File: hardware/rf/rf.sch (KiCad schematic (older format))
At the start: 47 parts, among them J1 Conn_02x14_Odd_Even, J2 SMP, J3 SMP, J4 SMP, U1 ECS-2520S33-400, U2 LMX2491, U3 BGT24MTR12

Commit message: Added BGT24 module castellation footprint, 3d model for 40MHz XO. Edits to schematic and pinouts based on layout of module. Initial parts placement and routing complete.
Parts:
- removed J1: Conn_02x14_Odd_Even, symbol Connector_Generic:Conn_02x14_Odd_Even
- removed R1, R3, R9: 0, Resistor_SMD:R_0402_1005Metric, symbol Device:R_US
- added J1: BGT24_Module_Castellations, bloop:BGT24_Module_Castellations, symbol bloop:BGT24_Module_Castellations
- C1, C12, C13, C15, C16, C17, C18, C2, C20, C21, C24, C25, C3, C4, C5, C6, C7, C8, C9: footprint Capacitor_SMD:C_0402_1005Metric -> Capacitor_SMD:C_0201_0603Metric
- R10, R2, R4, R5, R7, R8: footprint Resistor_SMD:R_0402_1005Metric -> Capacitor_SMD:C_0201_0603Metric
- R6: footprint Resistor_SMD:R_0402_1005Metric -> Capacitor_SMD:C_0402_1005Metric
- U1: footprint Crystal:Crystal_SMD_2520-4Pin_2.5x2.0mm -> bloop:Crystal_SMD_2520-4Pin_2.5x2.0mm
- U2: footprint Package_DFN_QFN:VQFN-24-1EP_4x4mm_P0.5mm_EP2.45x2.45mm -> Package_DFN_QFN:VQFN-24-1EP_4x4mm_P0.5mm_EP2.45x2.45mm_ThermalVias
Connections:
- wire segments 271 -> 259
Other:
- note added: "IF1 I/Q"
- note added: "IF2 I/Q"
- note added: "RF and PLL \npower isolated"
- note removed: "I/Q"
- moved on the sheet: C12, C14, C19, C20, C21, FB1, FB2, FB3

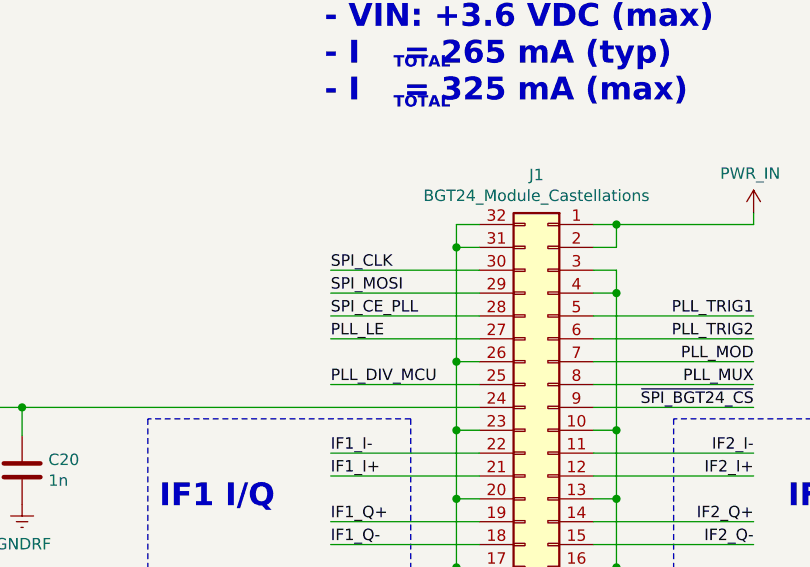
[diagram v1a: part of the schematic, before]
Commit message: Added 85305-0232 footprint for SMT SMP connector
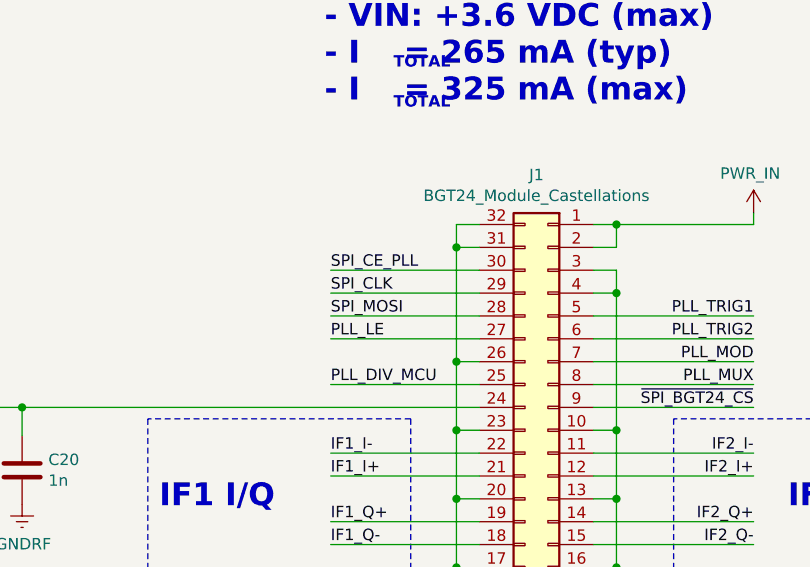
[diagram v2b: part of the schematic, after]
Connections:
- net SPI_CE_PLL: now also J1.30 (Pin_30); no longer J1.28 (Pin_28)
- net SPI_CLK: now also J1.29 (Pin_29); no longer J1.30 (Pin_30)
- net SPI_MOSI: now also J1.28 (Pin_28); no longer J1.29 (Pin_29)
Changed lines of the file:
@@
 Wire Wire Line
 	7750 2600 7975 2600
+Text Label 8800 7450 0    50   ~ 0
+SPI_CE_PLL
+Text Label 8800 7550 0    50   ~ 0
+SPI_CLK
 Text Label 8800 7650 0    50   ~ 0
-SPI_CE_PLL
-Text Label 8800 7450 0    50   ~ 0
-SPI_CLK
-Text Label 8800 7550 0    50   ~ 0
 SPI_MOSI
 Text Label 8800 7750 0    50   ~ 0
@@
 Connection ~ 9350 8750
 Wire Wire Line
-	8800 7550 9450 7550
-Wire Wire Line
-	9450 7450 8800 7450
-Wire Wire Line
 	8800 7650 9450 7650
 Wire Wire Line
+	9450 7550 8800 7550
+Wire Wire Line
+	8800 7450 9450 7450
+Wire Wire Line
 	9450 7750 8800 7750

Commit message: Replaced TH SMP connectors with SMT
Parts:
- J2, J3, J4: footprint bloop:0734153320 -> bloop:85305-0232
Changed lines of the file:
@@
 F 0 "J2" H 15957 3201 50  0000 L CNN
 F 1 "SMP" H 16060 2920 50  0000 L CNN
-F 2 "bloop:0734153320" H 16000 3050 50  0001 C CNN
+F 2 "bloop:85305-0232" H 16000 3050 50  0001 C CNN
 F 3 " ~" H 16000 3050 50  0001 C CNN
 	1    16000 3050
@@
 F 0 "J3" H 15957 3951 50  0000 L CNN
 F 1 "SMP" H 16060 3670 50  0000 L CNN
-F 2 "bloop:0734153320" H 16000 3800 50  0001 C CNN
+F 2 "bloop:85305-0232" H 16000 3800 50  0001 C CNN
 F 3 " ~" H 16000 3800 50  0001 C CNN
 	1    16000 3800
@@
 F 0 "J4" H 15957 4751 50  0000 L CNN
 F 1 "SMP" H 16060 4470 50  0000 L CNN
-F 2 "bloop:0734153320" H 16000 4600 50  0001 C CNN
+F 2 "bloop:85305-0232" H 16000 4600 50  0001 C CNN
 F 3 " ~" H 16000 4600 50  0001 C CNN
 	1    16000 4600

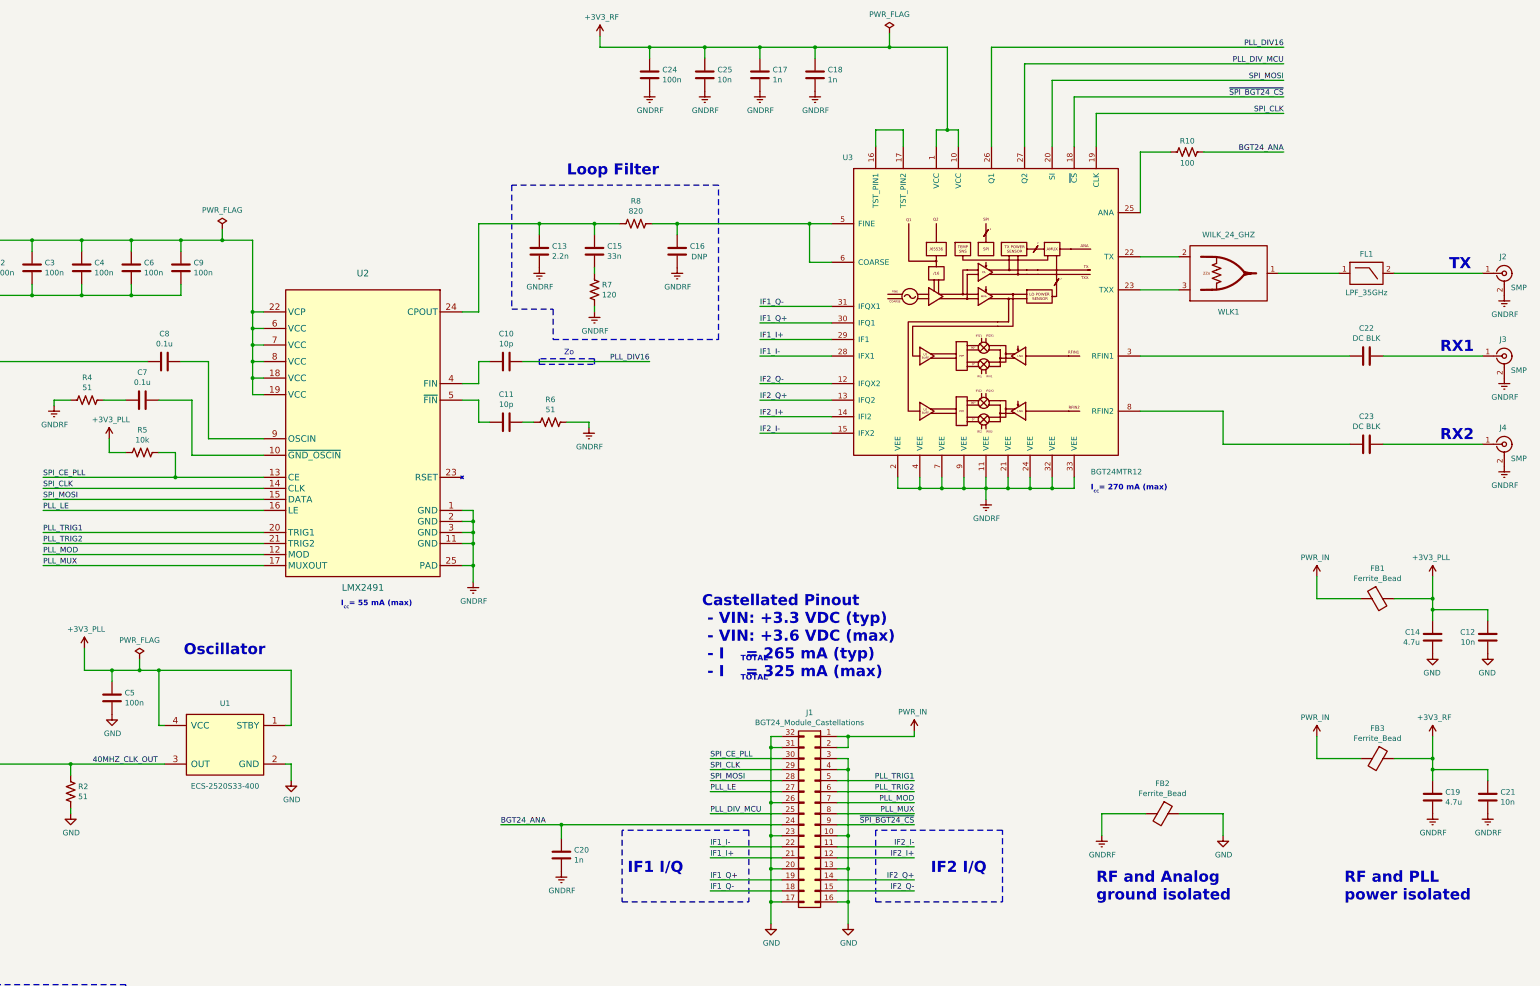
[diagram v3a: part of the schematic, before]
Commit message: Add 30 mil mask; update schematic for connector orientation
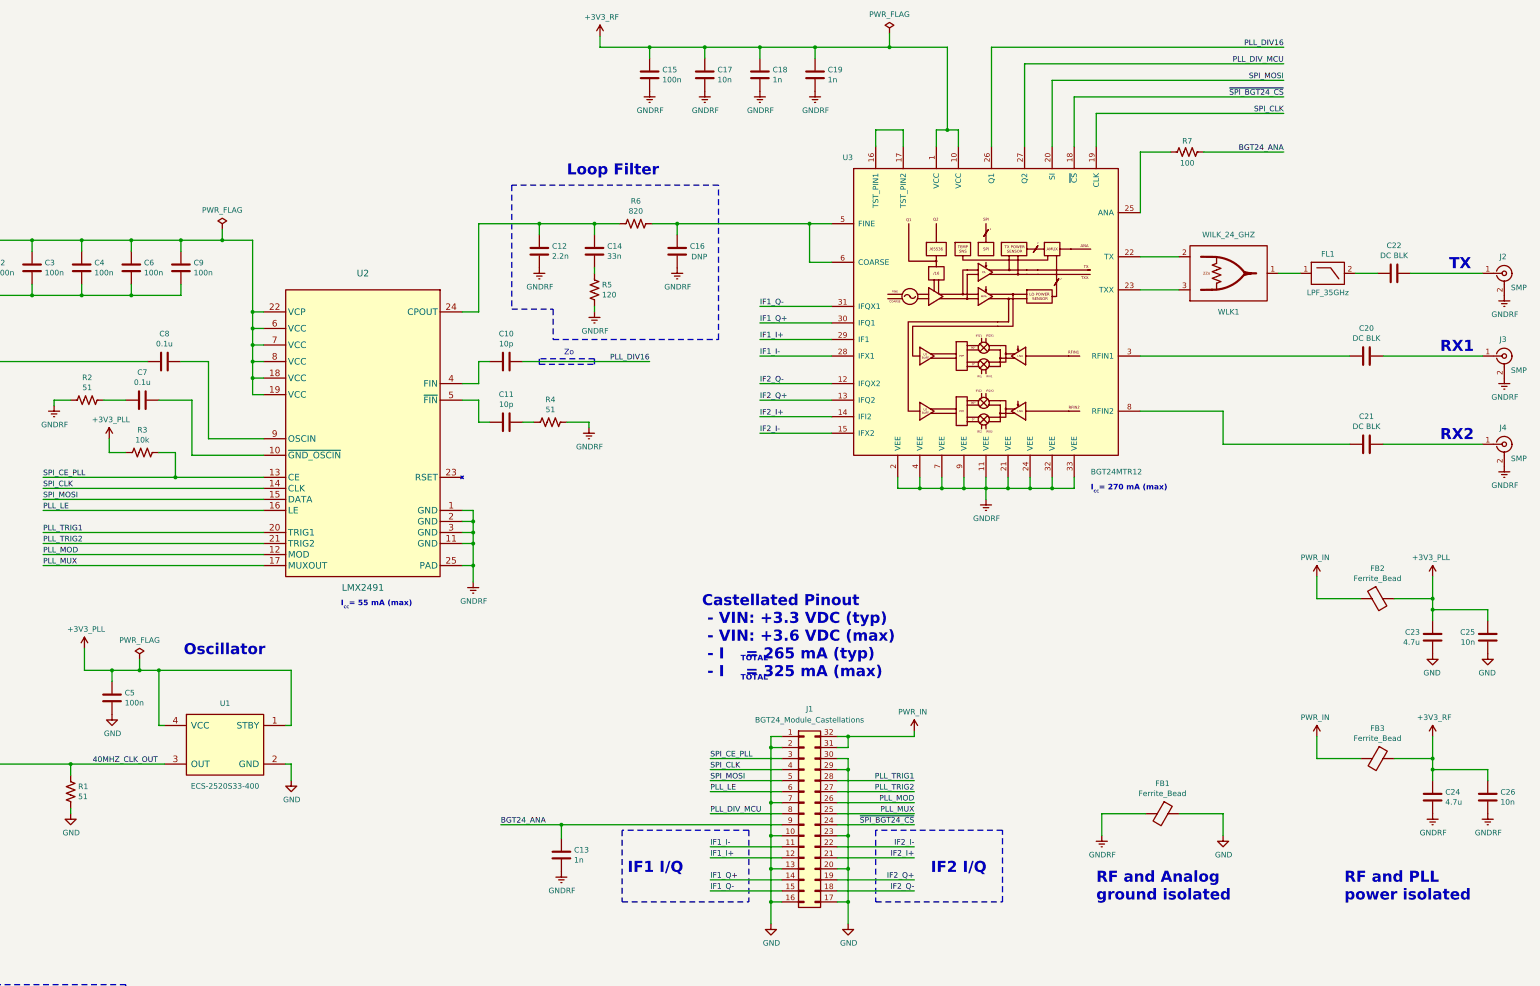
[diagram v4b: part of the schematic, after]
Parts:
- added C22: DC BLK, bloop:DC_Block, symbol Device:C
- renumbered C13 to C12, C20 to C13, C15 to C14, C24 to C15, C25 to C17, C17 to C18, C18 to C19, C22 to C20, C23 to C21, C14 to C23, C19 to C24, C12 to C25, C21 to C26, FB2 to FB1, FB1 to FB2, R2 to R1, R4 to R2, R5 to R3, R6 to R4, R7 to R5, R8 to R6, R10 to R7
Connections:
- net BGT24_ANA: now also J1.9 (Pin_9); no longer J1.24 (Pin_24)
- net GND: now also J1.1 (Pin_1), J1.2 (Pin_2), J1.29 (Pin_29), J1.30 (Pin_30), J1.7 (Pin_7); no longer J1.26 (Pin_26), J1.3 (Pin_3), J1.31 (Pin_31), J1.32 (Pin_32), J1.4 (Pin_4)
- net IF1_I+: now also J1.12 (Pin_12); no longer J1.21 (Pin_21)
- net IF1_I-: now also J1.11 (Pin_11); no longer J1.22 (Pin_22)
- net IF1_Q+: now also J1.14 (Pin_14); no longer J1.19 (Pin_19)
- net IF1_Q-: now also J1.15 (Pin_15); no longer J1.18 (Pin_18)
- net IF2_I+: now also J1.21 (Pin_21); no longer J1.12 (Pin_12)
- net IF2_I-: now also J1.22 (Pin_22); no longer J1.11 (Pin_11)
- net IF2_Q+: now also J1.19 (Pin_19); no longer J1.14 (Pin_14)
- net IF2_Q-: now also J1.18 (Pin_18); no longer J1.15 (Pin_15)
- net PLL_DIV_MCU: now also J1.8 (Pin_8); no longer J1.25 (Pin_25)
- net PLL_LE: now also J1.6 (Pin_6); no longer J1.27 (Pin_27)
- net PLL_MOD: now also J1.26 (Pin_26); no longer J1.7 (Pin_7)
- net PLL_MUX: now also J1.25 (Pin_25); no longer J1.8 (Pin_8)
- net PLL_TRIG1: now also J1.28 (Pin_28); no longer J1.5 (Pin_5)
- net PLL_TRIG2: now also J1.27 (Pin_27); no longer J1.6 (Pin_6)
- net PWR_IN: now also J1.31 (Pin_31), J1.32 (Pin_32); no longer J1.1 (Pin_1), J1.2 (Pin_2)
- net SPI_CE_PLL: now also J1.3 (Pin_3); no longer J1.30 (Pin_30)
- net SPI_CLK: now also J1.4 (Pin_4); no longer J1.29 (Pin_29)
- net SPI_MOSI: now also J1.5 (Pin_5); no longer J1.28 (Pin_28)
- net ~SPI_BGT24_CS: now also J1.24 (Pin_24); no longer J1.9 (Pin_9)
- net at J2.1 (In): now also C22.1; no longer FL1.2 (OUT)
- new net: C22.2, FL1.2 (OUT)
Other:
- moved on the sheet: FL1
